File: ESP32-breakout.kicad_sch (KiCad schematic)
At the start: 23 parts, among them IC1 ESP32-S2-MINI-2U-N4, J1 UJ20-C-H-G-SMT-1-P16-TR, J2 530480310, SW3 SW_MEC_5E, SW4 SW_MEC_5E, U1 STUSB4500QTR, U2 TJA1051T-3, U3 UA78M33CDCYRG3, U7 MP9361DJ-LF-Z

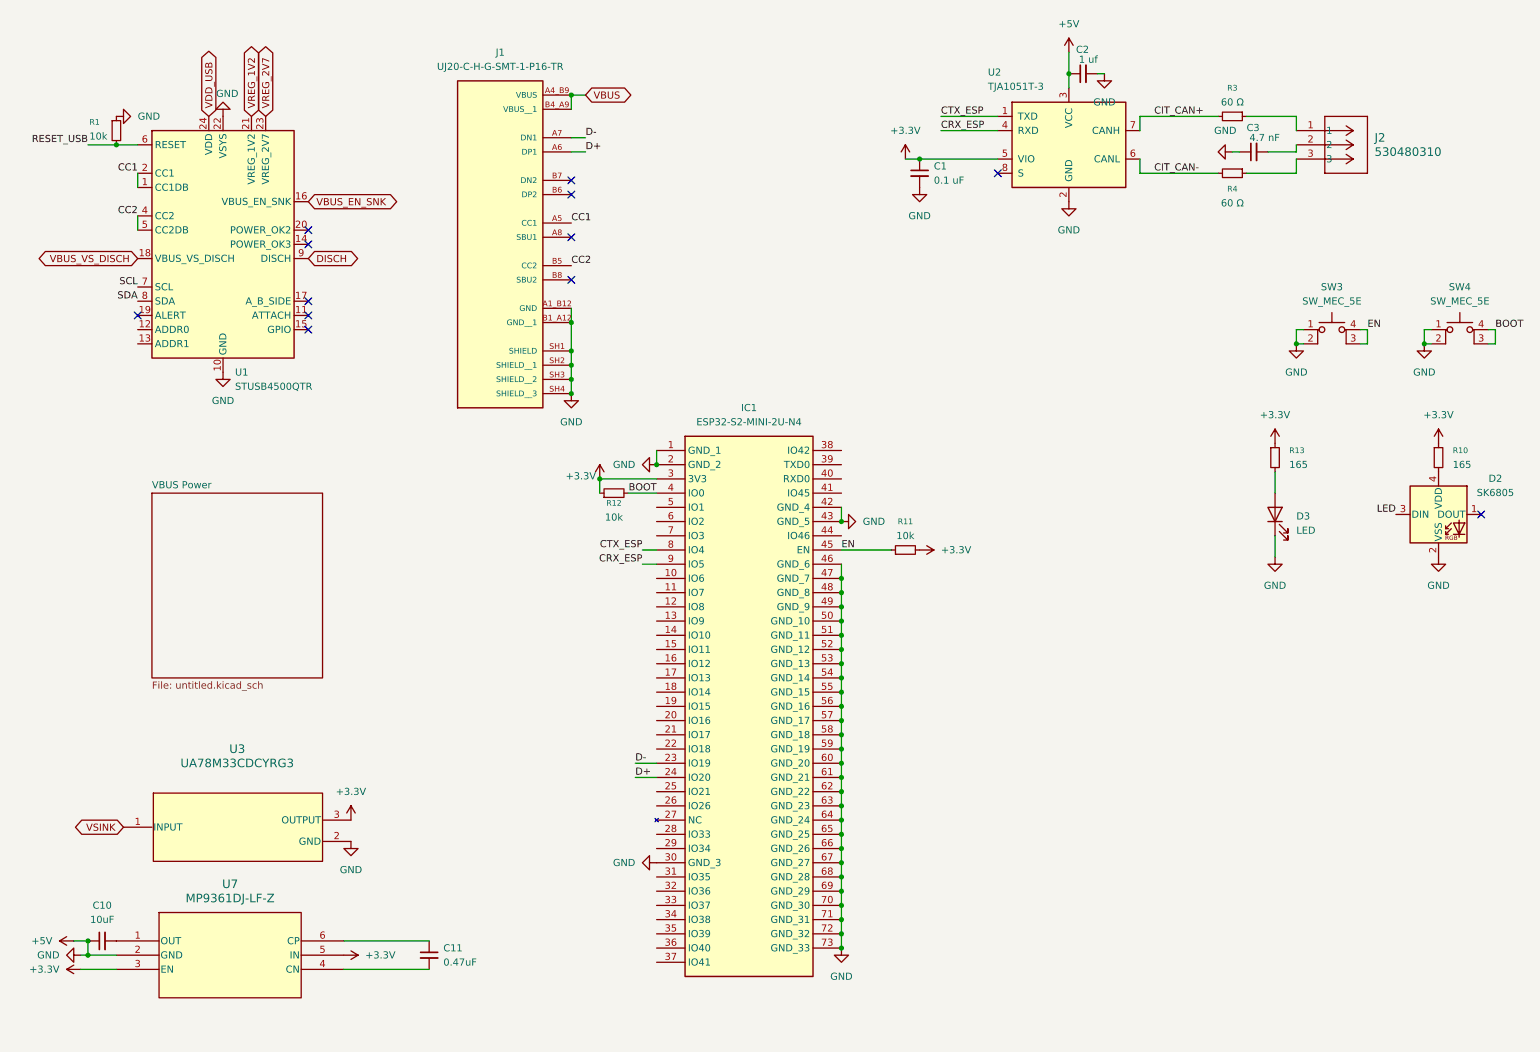
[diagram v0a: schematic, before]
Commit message: Updated schematic to improve layout
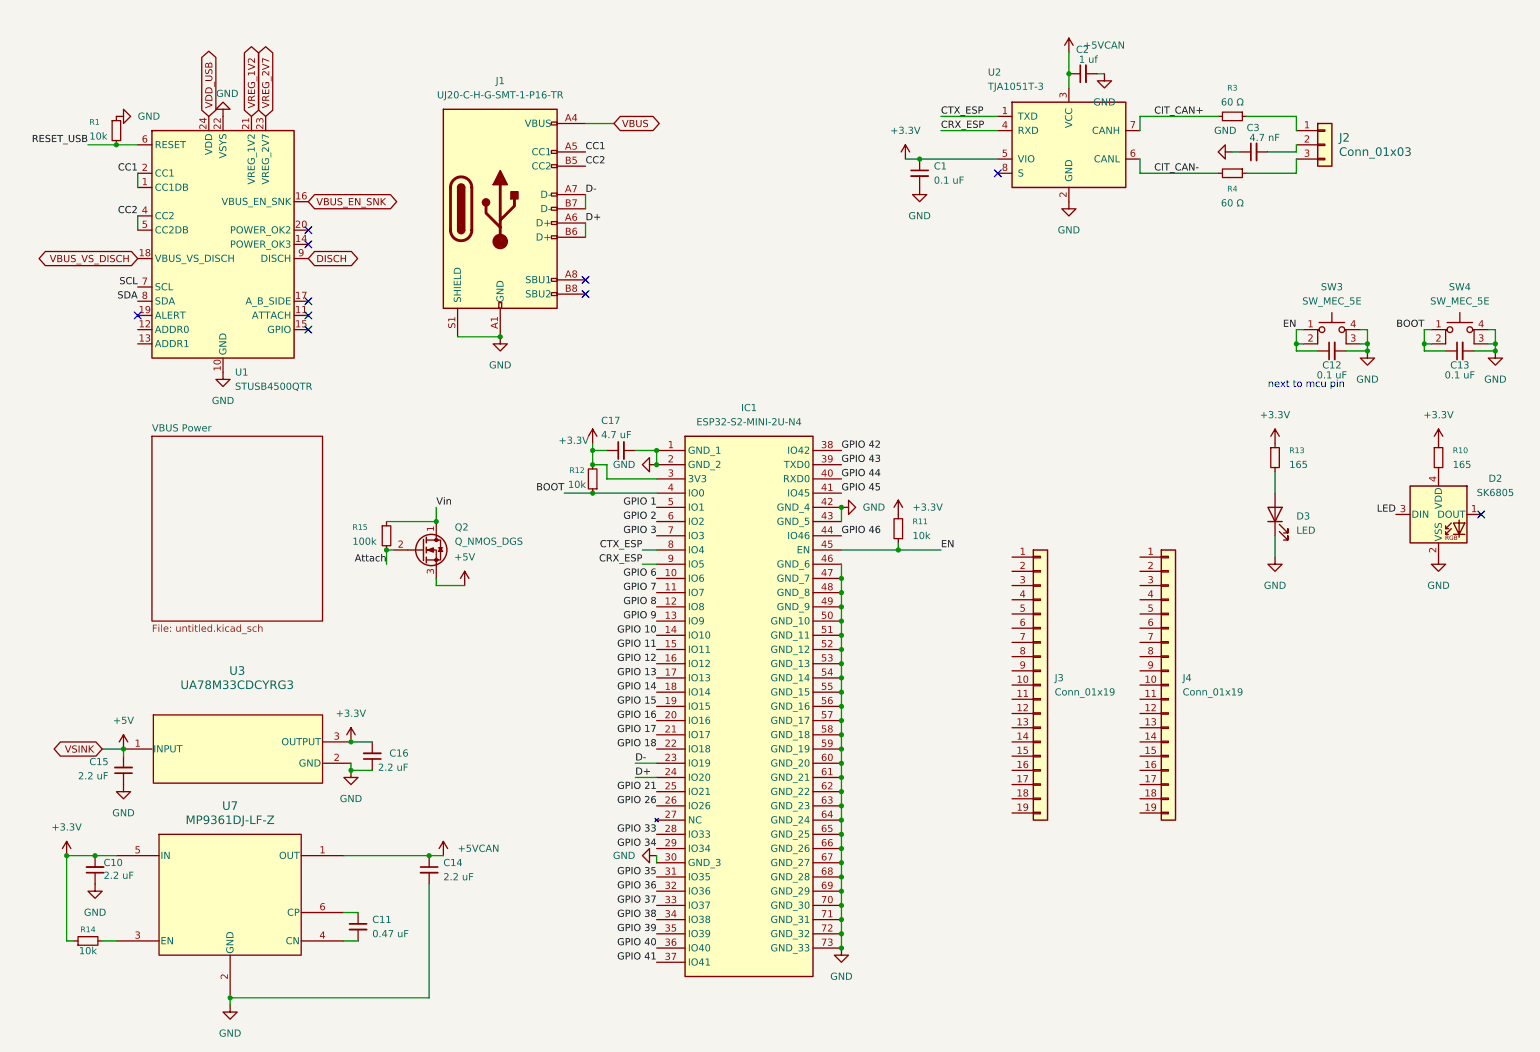
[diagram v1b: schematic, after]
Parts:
- added C12, C13: 0.1 uF, Capacitor_SMD:C_0603_1608Metric_Pad1.08x0.95mm_HandSolder, symbol Device:C_Small
- added C14, C15, C16: 2.2 uF, Capacitor_SMD:C_0603_1608Metric_Pad1.08x0.95mm_HandSolder, symbol Device:C_Small
- added C17: 4.7 uF, Capacitor_SMD:C_0603_1608Metric_Pad1.08x0.95mm_HandSolder, symbol Device:C_Small
- added J3, J4: Conn_01x19, Connector_PinHeader_2.54mm:PinHeader_1x19_P2.54mm_Vertical, symbol Connector_Generic:Conn_01x19
- added Q2: Q_NMOS_DGS, symbol Transistor_FET:Q_NMOS_DGS
- added R14: 10k, Resistor_SMD:R_0603_1608Metric_Pad0.98x0.95mm_HandSolder, symbol Device:R_Small
- added R15: 100k, symbol Device:R_Small
- C10: value 10uF -> 2.2 uF
- C11: value 0.47uF -> 0.47 uF
- J1: symbol UJ20-C-H-G-SMT-1-P16-TR:UJ20-C-H-G-SMT-1-P16-TR -> Connector:USB_C_Receptacle_USB2.0_16P
- J2: value 530480310 -> Conn_01x03; footprint Jayse_Footprints:CONN03_530480310_MOL -> Jayse_Footprints:CONN_S3B-ZR_JST; symbol 2026-06-30_20-34-03:530480310 -> Connector_Generic:Conn_01x03
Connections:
- net VSINK is gone; now on net +5V: U3.1 (INPUT)
- net +3.3V: now also C10.2, R12.2, C16.2, C17.1, R14.1; no longer R12.1, U7.3 (EN)
- net +5V: now also C15.2, Q2.3 (S); no longer C1.2, C10.1, C2.1, C2.2, C3.1, D2.2 (VSS), D3.1 (K), IC1.1 (GND_1), IC1.2 (GND_2), IC1.30 (GND_3), IC1.42 (GND_4), IC1.43 (GND_5), IC1.46 (GND_6), IC1.47 (GND_7), IC1.48 (GND_8), IC1.49 (GND_9), IC1.50 (GND_10), IC1.51 (GND_11), IC1.52 (GND_12), IC1.53 (GND_13), IC1.54 (GND_14), IC1.55 (GND_15), IC1.56 (GND_16), IC1.57 (GND_17), IC1.58 (GND_18), IC1.59 (GND_19), IC1.60 (GND_20), IC1.61 (GND_21), IC1.62 (GND_22), IC1.63 (GND_23), IC1.64 (GND_24), IC1.65 (GND_25), IC1.66 (GND_26), IC1.67 (GND_27), IC1.68 (GND_28), IC1.69 (GND_29), IC1.70 (GND_30), IC1.71 (GND_31), IC1.72 (GND_32), IC1.73 (GND_33), J1.A1_B12 (GND), J1.B1_A12 (GND__1), J1.SH1 (SHIELD), J1.SH2 (SHIELD__1), J1.SH3 (SHIELD__2), J1.SH4 (SHIELD__3), R1.1, SW3.1, SW3.2, SW4.1, SW4.2, U1.10 (GND), U1.22 (VSYS), U1.25 (GND), U2.2 (GND), U2.3 (VCC), U3.2 (GND), U3.4 (GND), U7.2 (GND)
- net BOOT: now also R12.1, SW4.1, SW4.2, C13.1; no longer R12.2, SW4.3 (K), SW4.4 (A)
- net D+: now also J1.B6 (D+)
- net D-: now also J1.B7 (D-)
- net EN: now also SW3.1, SW3.2, C12.1; no longer SW3.3 (K), SW3.4 (A)
- net VBUS: now also J1.A4 (VBUS), J1.A9 (VBUS), J1.B4 (VBUS), J1.B9 (VBUS); no longer J1.A4_B9 (VBUS), J1.B4_A9 (VBUS__1)
- net GPIO 6: now reaches IC1.10 (IO6)
- net GPIO 7: now reaches IC1.11 (IO7)
- net GPIO 8: now reaches IC1.12 (IO8)
- net GPIO 9: now reaches IC1.13 (IO9)
- net GPIO 10: now reaches IC1.14 (IO10)
- net GPIO 11: now reaches IC1.15 (IO11)
- net GPIO 12: now reaches IC1.16 (IO12)
- net GPIO 13: now reaches IC1.17 (IO13)
- net GPIO 14: now reaches IC1.18 (IO14)
- net GPIO 15: now reaches IC1.19 (IO15)
- net GPIO 16: now reaches IC1.20 (IO16)
- net GPIO 17: now reaches IC1.21 (IO17)
- net GPIO 18: now reaches IC1.22 (IO18)
- net GPIO 21: now reaches IC1.25 (IO21)
- net GPIO 26: now reaches IC1.26 (IO26)
- net GPIO 33: now reaches IC1.28 (IO33)
- net GPIO 34: now reaches IC1.29 (IO34)
- net GPIO 35: now reaches IC1.31 (IO35)
- net GPIO 36: now reaches IC1.32 (IO36)
- net GPIO 37: now reaches IC1.33 (IO37)
- net GPIO 38: now reaches IC1.34 (IO38)
- net GPIO 39: now reaches IC1.35 (IO39)
- net GPIO 40: now reaches IC1.36 (IO40)
- net GPIO 41: now reaches IC1.37 (IO41)
- net GPIO 42: now reaches IC1.38 (IO42)
- net GPIO 43: now reaches IC1.39 (TXD0)
- net GPIO 44: now reaches IC1.40 (RXD0)
- net GPIO 45: now reaches IC1.41 (IO45)
- net GPIO 46: now reaches IC1.44 (IO46)
- net GPIO 1: now reaches IC1.5 (IO1)
- net GPIO 2: now reaches IC1.6 (IO2)
- net GPIO 3: now reaches IC1.7 (IO3)
- net +5VCAN: now reaches U7.1 (OUT)
- net +5VCAN: now also C2.1, U2.3 (VCC), C14.1; no longer C10.2
- new net: R14.2, U7.3 (EN)
- new net Attach: Q2.2 (G), R15.2
- new net GND: C1.2, C10.1, C12.2, C13.2, C14.2, C15.1, C16.1, C17.2, C2.2, C3.1, D2.2 (VSS), D3.1 (K), IC1.1 (GND_1), IC1.2 (GND_2), IC1.30 (GND_3), IC1.42 (GND_4), IC1.43 (GND_5), IC1.46 (GND_6), IC1.47 (GND_7), IC1.48 (GND_8), IC1.49 (GND_9), IC1.50 (GND_10), IC1.51 (GND_11), IC1.52 (GND_12), IC1.53 (GND_13), IC1.54 (GND_14), IC1.55 (GND_15), IC1.56 (GND_16), IC1.57 (GND_17), IC1.58 (GND_18), IC1.59 (GND_19), IC1.60 (GND_20), IC1.61 (GND_21), IC1.62 (GND_22), IC1.63 (GND_23), IC1.64 (GND_24), IC1.65 (GND_25), IC1.66 (GND_26), IC1.67 (GND_27), IC1.68 (GND_28), IC1.69 (GND_29), IC1.70 (GND_30), IC1.71 (GND_31), IC1.72 (GND_32), IC1.73 (GND_33), J1.A1 (GND), J1.A12 (GND), J1.B1 (GND), J1.B12 (GND), J1.S1 (SHIELD), R1.1, SW3.3 (K), SW3.4 (A), SW4.3 (K), SW4.4 (A), U1.10 (GND), U1.22 (VSYS), U1.25 (GND), U2.2 (GND), U3.2 (GND), U3.4 (GND), U7.2 (GND)
- new net Vin: Q2.1 (D), R15.1
- no-connect marks 12 -> 10
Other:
- note added: "next to mcu pin"
- moved on the sheet: R11, R12, U3, U7

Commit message: Changed power regulator and finished everything except pin headers
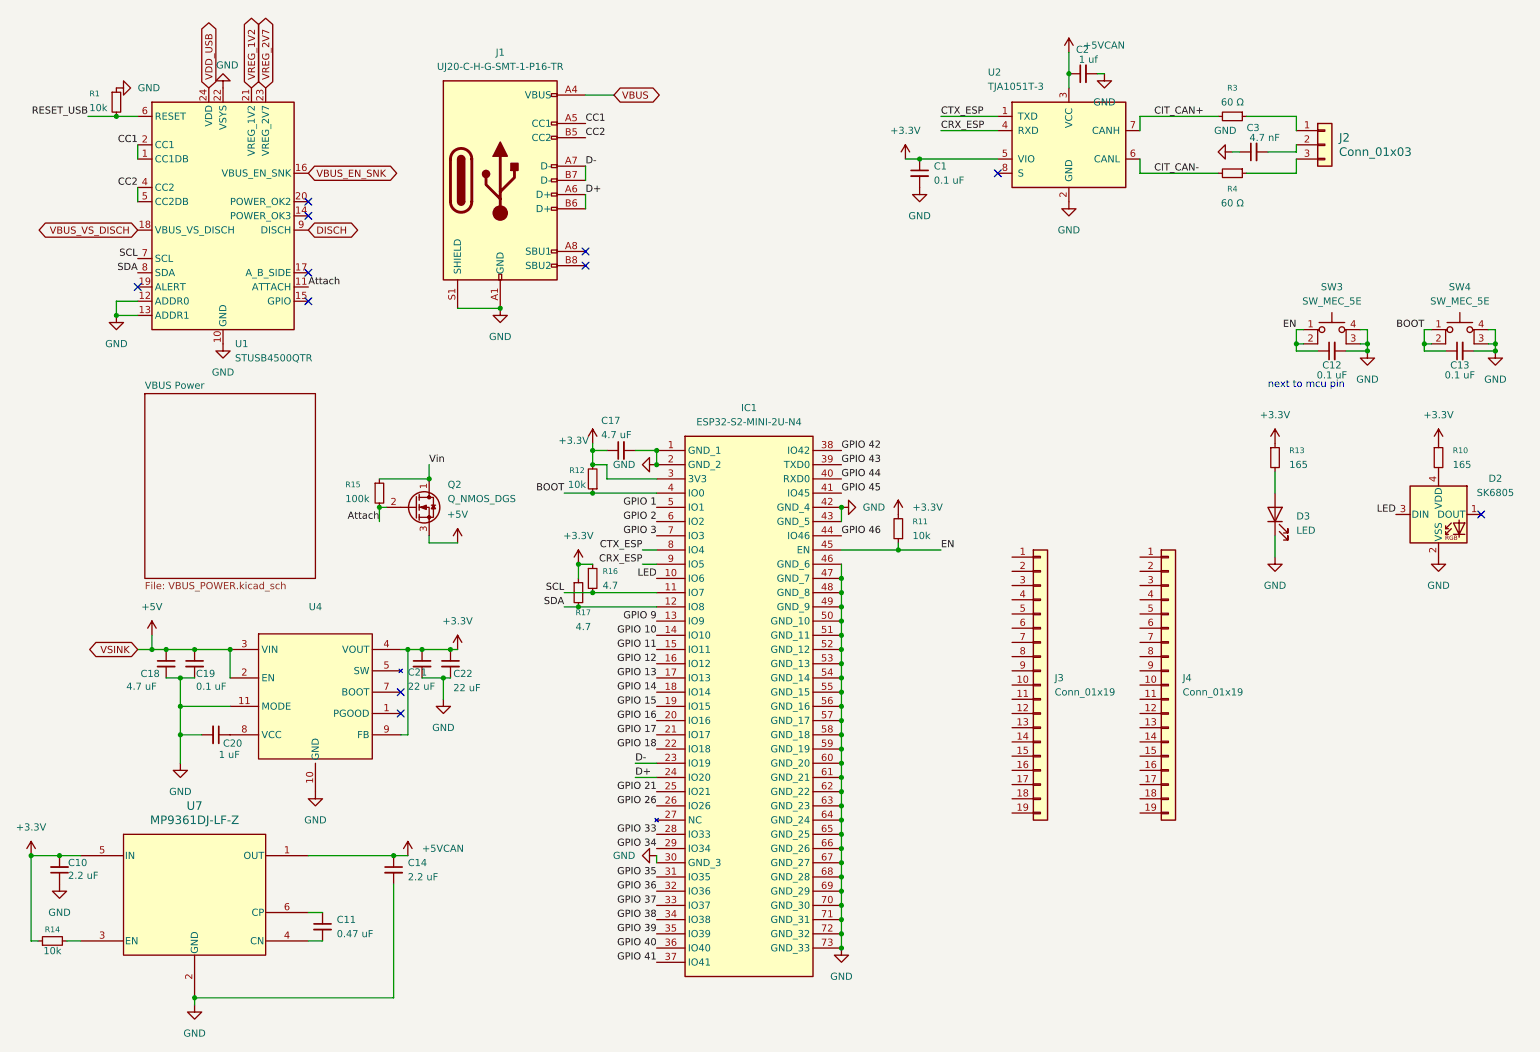
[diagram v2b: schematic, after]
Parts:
- removed C15, C16: 2.2 uF, Capacitor_SMD:C_0603_1608Metric_Pad1.08x0.95mm_HandSolder, symbol Device:C_Small
- removed U3: UA78M33CDCYRG3, Jayse_Footprints:DCY0004A_N, symbol 2026-06-29_19-04-53:UA78M33CDCYRG3
- added C18: 4.7 uF, symbol Device:C_Small
- added C19: 0.1 uF, symbol Device:C_Small
- added C20: 1 uF, symbol Device:C_Small
- added C21, C22: 22 uF, symbol Device:C_Small
- added R16, R17: 4.7, symbol Device:R_Small
- added U4: ~, TPSM33606S3QRDNRQ1:TPSM33606S3QRDNRQ1, symbol TPSM33606S3QRDNRQ1:TPSM33606S3QRDNRQ1
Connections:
- net GPIO 6 is gone; now on net LED: IC1.10 (IO6)
- net GPIO 7 is gone; now on net SCL: IC1.11 (IO7)
- net GPIO 8 is gone; now on net SDA: IC1.12 (IO8)
- net +3.3V: now also C21.1, C22.1, R16.1, R17.1, U4.4 (VOUT), U4.9 (FB)
- net +5V: now also C18.1, C19.1, U4.2 (EN), U4.3 (VIN)
- net Attach: now also U1.11 (ATTACH)
- net GND: now also U1.12 (ADDR0), U1.13 (ADDR1), C18.2, C19.2, C20.2, C21.2, C22.2, U4.10 (GND), U4.11 (MODE)
- net SCL: now also R16.2
- net SDA: now also R17.2
- new net: U4.5 (SW), U4.6 (SW)
- new net: C20.1, U4.8 (VCC)
- no-connect marks 10 -> 11
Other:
- sheet VBUS Power: file untitled.kicad_sch -> VBUS_POWER.kicad_sch
- moved on the sheet: C10, C11, C14, J1, Q2, R1, R14, R15, U1, U7

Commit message: Updated to KiCad 10
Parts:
- C18, C19, C20, C21, C22: footprint (none) -> Capacitor_SMD:C_0603_1608Metric_Pad1.08x0.95mm_HandSolder
- Q2: footprint (none) -> Package_TO_SOT_SMD:SOT-23-3
- R15, R16, R17: footprint (none) -> Resistor_SMD:R_0603_1608Metric_Pad0.98x0.95mm_HandSolder
- U4: value ~ -> TPSM33606S3QRDNRQ1

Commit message: Began initial PCB layout
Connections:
- net at J2.1 (Pin_1): now also R4.1; no longer R3.1
- net at J2.3 (Pin_3): now also R3.1; no longer R4.1
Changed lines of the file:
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@@
 		(in_pos_files yes)
 		(dnp no)
-		(fields_autoplaced yes)
 		(property "Reference" "#PWR015"
 			(at 201.93 25.4 0)
@@
 		)
 		(property "Value" "+5VCAN"
-			(at 204.47 20.3199 0)
+			(at 202.184 18.034 0)
 			(show_name no)
 			(do_not_autoplace no)
@@
 		(lib_id "Connector_Generic:Conn_01x03")
 		(at 247.65 38.1 0)
+		(mirror x)
 		(unit 1)
 		(body_style 1)
@@
 		(in_pos_files yes)
 		(dnp no)
-		(fields_autoplaced yes)
 		(property "Reference" "J2"
-			(at 250.19 36.8299 0)
+			(at 250.19 39.3701 0)
 			(show_name no)
 			(do_not_autoplace no)
@@
 		)
 		(property "Value" "Conn_01x03"
-			(at 250.19 39.3699 0)
-			(show_name no)
-			(do_not_autoplace no)
+			(at 250.19 36.8301 0)
+			(show_name no)
+			(do_not_autoplace no)
